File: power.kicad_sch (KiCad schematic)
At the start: 32 parts, among them SW1 SW_SPDT, U14 BH-18650-B5BA016

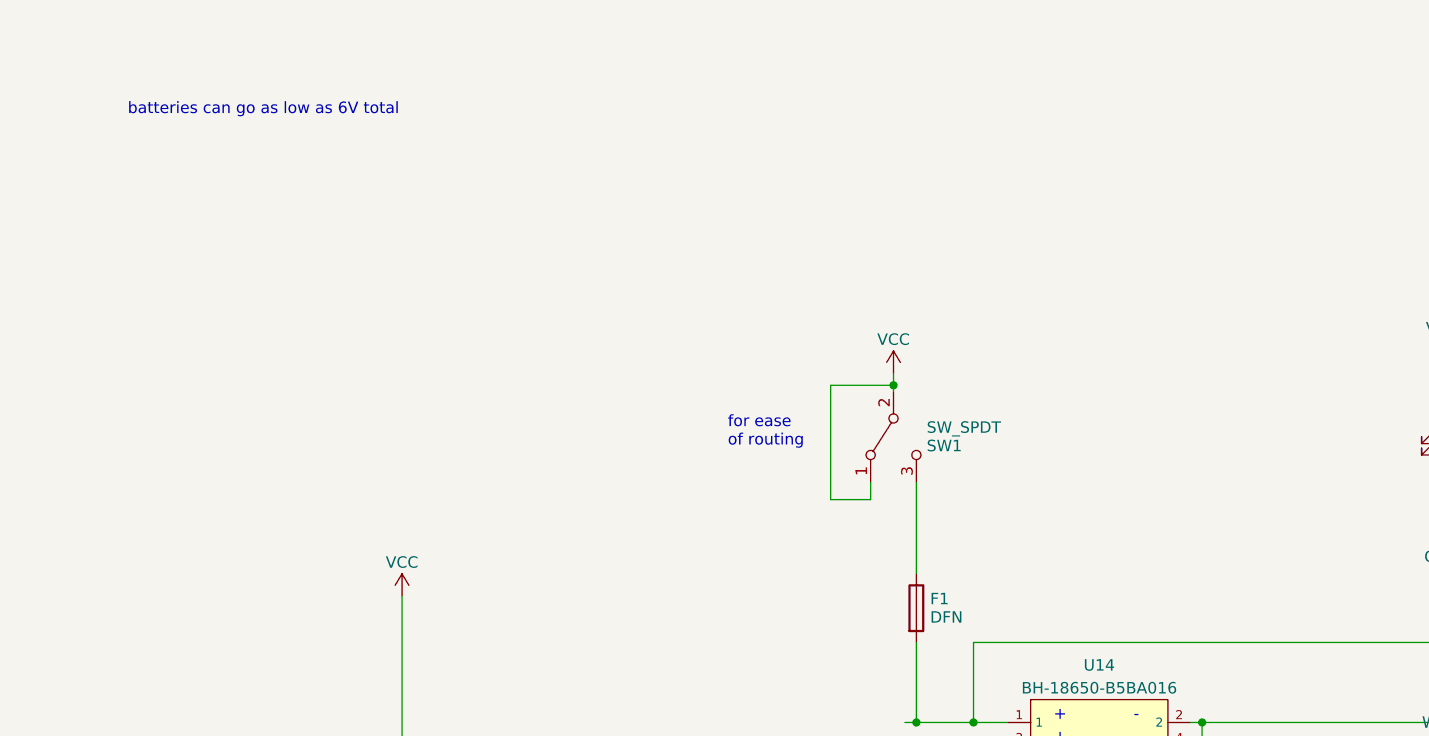
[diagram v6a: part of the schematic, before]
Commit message: specified correct shift register
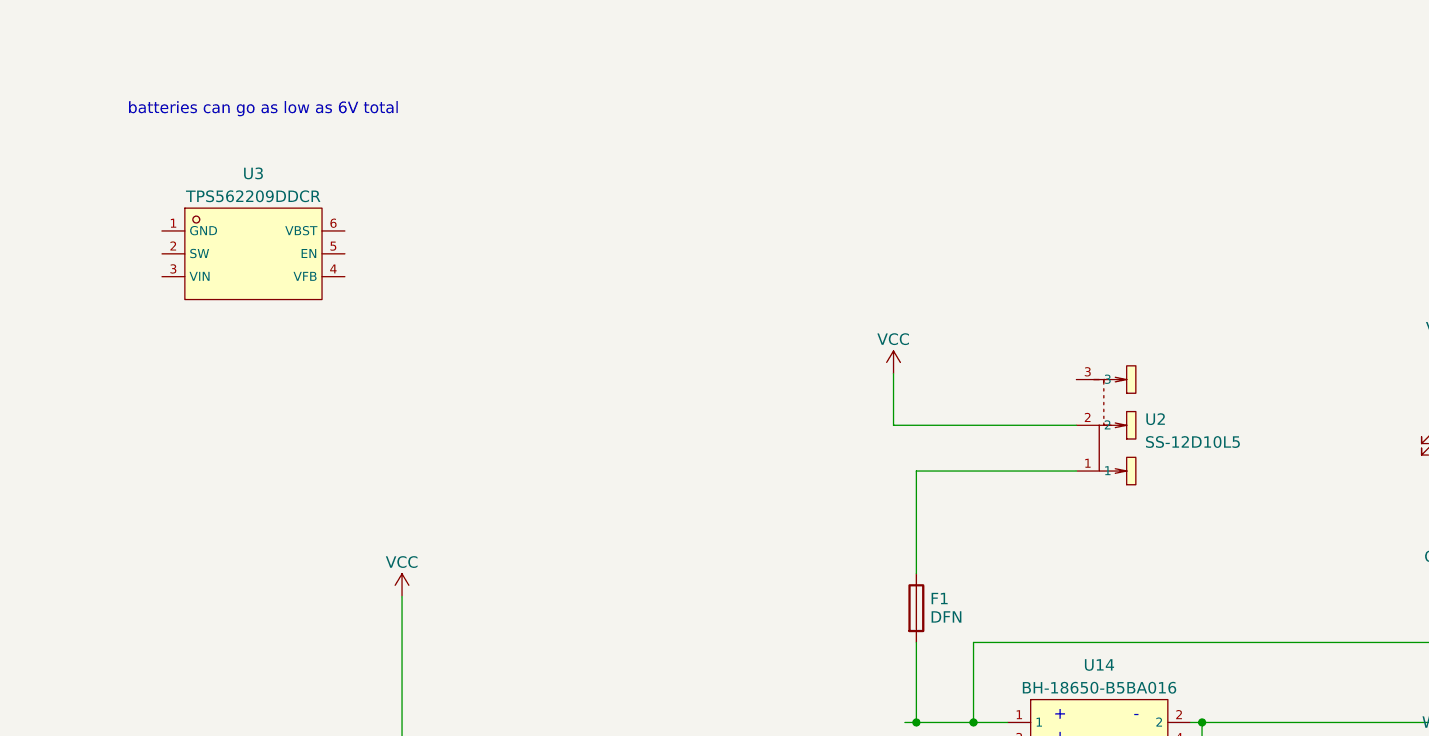
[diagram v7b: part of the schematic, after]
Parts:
- removed SW1: SW_SPDT, switches:TSM1x3, symbol Switch:SW_SPDT
- added U2: SS-12D10L5, footprint:SW-TH_SS-12D10L5, symbol my_symbols:SS-12D10L5
- added U3: TPS562209DDCR, footprint:SOT-23-6_L2.9-W1.6-P0.95-LS2.8-BL, symbol my_symbols:TPS562209DDCR
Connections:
- net VCC: now also U2.2
- net at F1.1: now also U2.1
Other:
- note removed: "for ease of routing"

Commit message: added more symbols
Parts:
- removed D?: WRONG!, Diode_SMD:D_0805_2012Metric_Pad1.15x1.40mm_HandSolder, symbol Device:LED
- removed R24: 4k, Resistor_SMD:R_0603_1608Metric_Pad0.98x0.95mm_HandSolder, symbol Device:R_Small
- removed U3: TPS562209DDCR, footprint:SOT-23-6_L2.9-W1.6-P0.95-LS2.8-BL, symbol my_symbols:TPS562209DDCR
- added C? (x4): 22u, Capacitor_SMD:C_0805_2012Metric_Pad1.18x1.45mm_HandSolder, symbol Device:C
- added C? (x3): 100n, Capacitor_SMD:C_0603_1608Metric_Pad1.08x0.95mm_HandSolder, symbol Device:C
- added D?: WRONG!, Diode_SMD:D_0805_2012Metric_Pad1.15x1.40mm_HandSolder, symbol Device:LED
- added R1: 1k, Resistor_SMD:R_0603_1608Metric_Pad0.98x0.95mm_HandSolder, symbol Device:R_Small
- added R? (x2): 10k, Resistor_SMD:R_0603_1608Metric_Pad0.98x0.95mm_HandSolder, symbol Device:R
- added R?: 56k, Resistor_SMD:R_0603_1608Metric_Pad0.98x0.95mm_HandSolder, symbol Device:R
- added U4: TPS562209DDCR, footprint:SOT-23-6_L2.9-W1.6-P0.95-LS2.8-BL, symbol my_symbols:TPS562209DDCR
- added U5: FXL0530-4R7-M, footprint:IND-SMD_L5.4-W5.2_FXL0530, symbol my_symbols:FXL0530-4R7-M
- D? (x2): JLCPCB Part# (none) -> C84256
- D?: JLCPCB Part# (none) -> C2297
- F1: JLCPCB Part# (none) -> C2760311
- Q? (x4): JLCPCB Part# (none) -> C20917
- R17, R20, R27: value 1k -> 220
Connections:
- net +5V: now also C?.1, C?.1, C?.1, C?.1, C?.1, C?.1, R?.2, U5.2
- net GND: now also C?.2, C?.2, C?.2, C?.2, C?.2, C?.2, R1.1, R?.1, U4.1 (GND)
- net VCC: now also R?.2, U4.3 (VIN)
- net at Q?.3 (D), Q?.3 (D), Q?.3 (D)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: now also D?.2 (A)
- net at R20.1: now also D?.1 (K)
- net 1S: now reaches D?.2 (A), R20.2, U14.4, U14.5
- net at D?.1 (K): now also R1.2
- new net: C?.1, U4.2 (SW), U5.1
- new net: C?.2, U4.6 (VBST)
- new net: R?.1, R?.2, U4.4 (VFB)
- new net: R?.1, U4.5 (EN)
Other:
- moved on the sheet: C?, F1, U2
